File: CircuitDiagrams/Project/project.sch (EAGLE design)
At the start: 105 parts, among them IC1 UC3C, IC2 PCA9542A, IC3 MT48LC4M16A2TSOP54, IC4 TB6593FNGSSOP20, IC5 TB6593FNGSSOP20, J2 1BY2THROUGHHOLE, J3 1BY2THROUGHHOLE, J4 1BY2THROUGHHOLE, Q1 OV7670, Q2 OV7670, Q3 VREGSOT-223, Q4 TCRT1010TH, Q5 TCRT1010TH, Q6 CSM-7X-DU, X2 MICROSDSMD

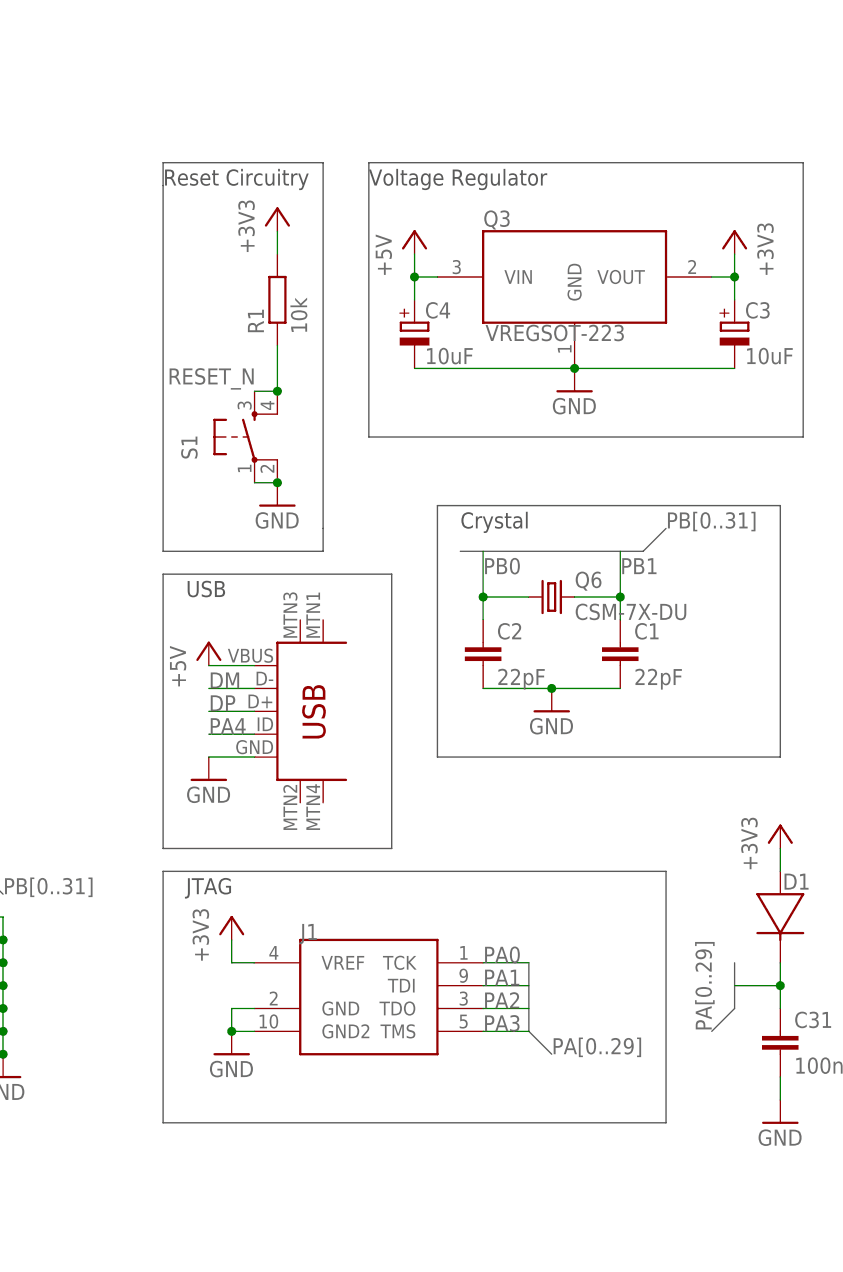
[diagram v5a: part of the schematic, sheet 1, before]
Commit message: Changed JTAG Connection to include the Reset Pin.
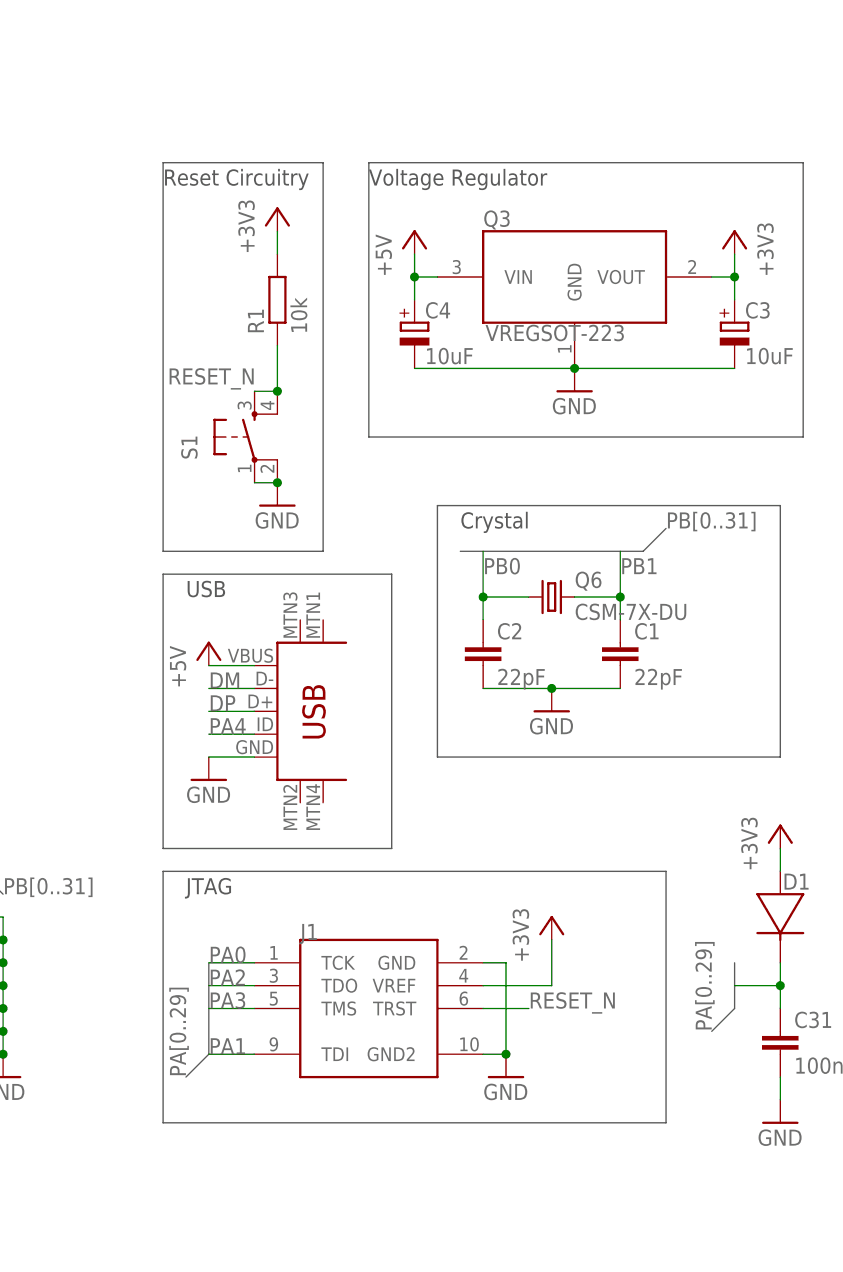
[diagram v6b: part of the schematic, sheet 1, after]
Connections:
- net RESET_N: now also J1.TRST
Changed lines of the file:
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@@
 <text x="134.62" y="60.96" size="1.778" layer="97">USB</text>
 <wire x1="132.08" y1="109.22" x2="149.86" y2="109.22" width="0.1524" layer="97"/>
-<wire x1="149.86" y1="109.22" x2="149.86" y2="68.58" width="0.1524" layer="97"/>
-<wire x1="149.86" y1="68.58" x2="149.86" y2="66.04" width="0.1524" layer="97"/>
+<wire x1="149.86" y1="109.22" x2="149.86" y2="66.04" width="0.1524" layer="97"/>
 <wire x1="149.86" y1="66.04" x2="132.08" y2="66.04" width="0.1524" layer="97"/>
-<wire x1="132.08" y1="66.04" x2="132.08" y2="106.68" width="0.1524" layer="97"/>
-<wire x1="132.08" y1="106.68" x2="132.08" y2="109.22" width="0.1524" layer="97"/>
+<wire x1="132.08" y1="66.04" x2="132.08" y2="109.22" width="0.1524" layer="97"/>
 <text x="132.08" y="106.68" size="1.778" layer="97">Reset Circuitry</text>
 <wire x1="154.94" y1="109.22" x2="203.2" y2="109.22" width="0.1524" layer="97"/>
@@
 <instance part="IC1" gate="G$1" x="50.8" y="58.42"/>
 <instance part="J1" gate="G$1" x="154.94" y="17.78"/>
-<instance part="+3V1" gate="G$1" x="139.7" y="25.4"/>
+<instance part="+3V1" gate="G$1" x="175.26" y="25.4"/>
 <instance part="+3V2" gate="G$1" x="-10.16" y="111.76"/>
 <instance part="GND1" gate="1" x="114.3" y="7.62"/>
-<instance part="GND2" gate="1" x="139.7" y="10.16"/>
+<instance part="GND2" gate="1" x="170.18" y="7.62"/>
 <instance part="U$1" gate="G$1" x="144.78" y="43.18"/>
 <instance part="GND3" gate="1" x="137.16" y="40.64"/>
@@
 </segment>
 <segment>
-<wire x1="172.72" y1="20.32" x2="172.72" y2="12.7" width="0.762" layer="92"/>
-<wire x1="172.72" y1="12.7" x2="175.26" y2="10.16" width="0.762" layer="92"/>
-<label x="175.26" y="10.16" size="1.778" layer="95"/>
+<wire x1="137.16" y1="20.32" x2="137.16" y2="10.16" width="0.762" layer="92"/>
+<wire x1="137.16" y1="10.16" x2="134.62" y2="7.62" width="0.762" layer="92"/>
+<label x="134.62" y="7.62" size="1.778" layer="95" rot="R90"/>
 </segment>
 <segment>
@@
 <nets>
 <net name="GND" class="0">
-<segment>
-<pinref part="J1" gate="G$1" pin="GND"/>
-<pinref part="GND2" gate="1" pin="GND"/>
-<wire x1="142.24" y1="15.24" x2="139.7" y2="15.24" width="0.1524" layer="91"/>
-<wire x1="139.7" y1="15.24" x2="139.7" y2="12.7" width="0.1524" layer="91"/>
-<pinref part="J1" gate="G$1" pin="GND2"/>
-<wire x1="142.24" y1="12.7" x2="139.7" y2="12.7" width="0.1524" layer="91"/>
-<junction x="139.7" y="12.7"/>
-</segment>
 <segment>
 <pinref part="IC1" gate="G$1" pin="GNDIO1"/>
@@
 <wire x1="200.66" y1="5.08" x2="200.66" y2="7.62" width="0.1524" layer="91"/>
 </segment>
+<segment>
+<pinref part="J1" gate="G$1" pin="GND2"/>
+<pinref part="GND2" gate="1" pin="GND"/>
+<wire x1="167.64" y1="10.16" x2="170.18" y2="10.16" width="0.1524" layer="91"/>
+<pinref part="J1" gate="G$1" pin="GND"/>
+<wire x1="167.64" y1="20.32" x2="170.18" y2="20.32" width="0.1524" layer="91"/>
+<wire x1="170.18" y1="20.32" x2="170.18" y2="10.16" width="0.1524" layer="91"/>
+<junction x="170.18" y="10.16"/>
+</segment>
 </net>
 <net name="+3V3" class="0">
@@
 <pinref part="+3V1" gate="G$1" pin="+3V3"/>
 <pinref part="J1" gate="G$1" pin="VREF"/>
-<wire x1="139.7" y1="22.86" x2="139.7" y2="20.32" width="0.1524" layer="91"/>
-<wire x1="139.7" y1="20.32" x2="142.24" y2="20.32" width="0.1524" layer="91"/>
+<wire x1="175.26" y1="22.86" x2="175.26" y2="17.78" width="0.1524" layer="91"/>
+<wire x1="175.26" y1="17.78" x2="167.64" y2="17.78" width="0.1524" layer="91"/>
 </segment>
 <segment>
@@
 <segment>
 <pinref part="J1" gate="G$1" pin="TCK"/>
-<wire x1="167.64" y1="20.32" x2="172.72" y2="20.32" width="0.1524" layer="91"/>
-<label x="167.64" y="20.32" size="1.778" layer="95"/>
+<wire x1="137.16" y1="20.32" x2="142.24" y2="20.32" width="0.1524" layer="91"/>
+<label x="137.16" y="20.32" size="1.778" layer="95"/>
 </segment>
 </net>
@@
 <segment>
 <pinref part="J1" gate="G$1" pin="TDI"/>
-<wire x1="167.64" y1="17.78" x2="172.72" y2="17.78" width="0.1524" layer="91"/>
-<label x="167.64" y="17.78" size="1.778" layer="95"/>
+<wire x1="142.24" y1="10.16" x2="137.16" y2="10.16" width="0.1524" layer="91"/>
+<label x="137.16" y="10.16" size="1.778" layer="95"/>
 </segment>
 </net>
@@
 <segment>
 <pinref part="J1" gate="G$1" pin="TDO"/>
-<wire x1="167.64" y1="15.24" x2="172.72" y2="15.24" width="0.1524" layer="91"/>
-<label x="167.64" y="15.24" size="1.778" layer="95"/>
+<wire x1="142.24" y1="17.78" x2="137.16" y2="17.78" width="0.1524" layer="91"/>
+<label x="137.16" y="17.78" size="1.778" layer="95"/>
 </segment>
 </net>
@@
 <segment>
 <pinref part="J1" gate="G$1" pin="TMS"/>
-<wire x1="172.72" y1="12.7" x2="167.64" y2="12.7" width="0.1524" layer="91"/>
-<label x="167.64" y="12.7" size="1.778" layer="95"/>
+<wire x1="142.24" y1="15.24" x2="137.16" y2="15.24" width="0.1524" layer="91"/>
+<label x="137.16" y="15.24" size="1.778" layer="95"/>
 </segment>
 </net>
@@
 <label x="132.588" y="84.582" size="1.778" layer="95"/>
 </segment>
-</net>
+<segment>
+<pinref part="J1" gate="G$1" pin="TRST"/>
+<wire x1="167.64" y1="15.24" x2="172.72" y2="15.24" width="0.1524" layer="91"/>
+<label x="172.72" y="15.24" size="1.778" layer="95"/>
+</segment>
+</net>

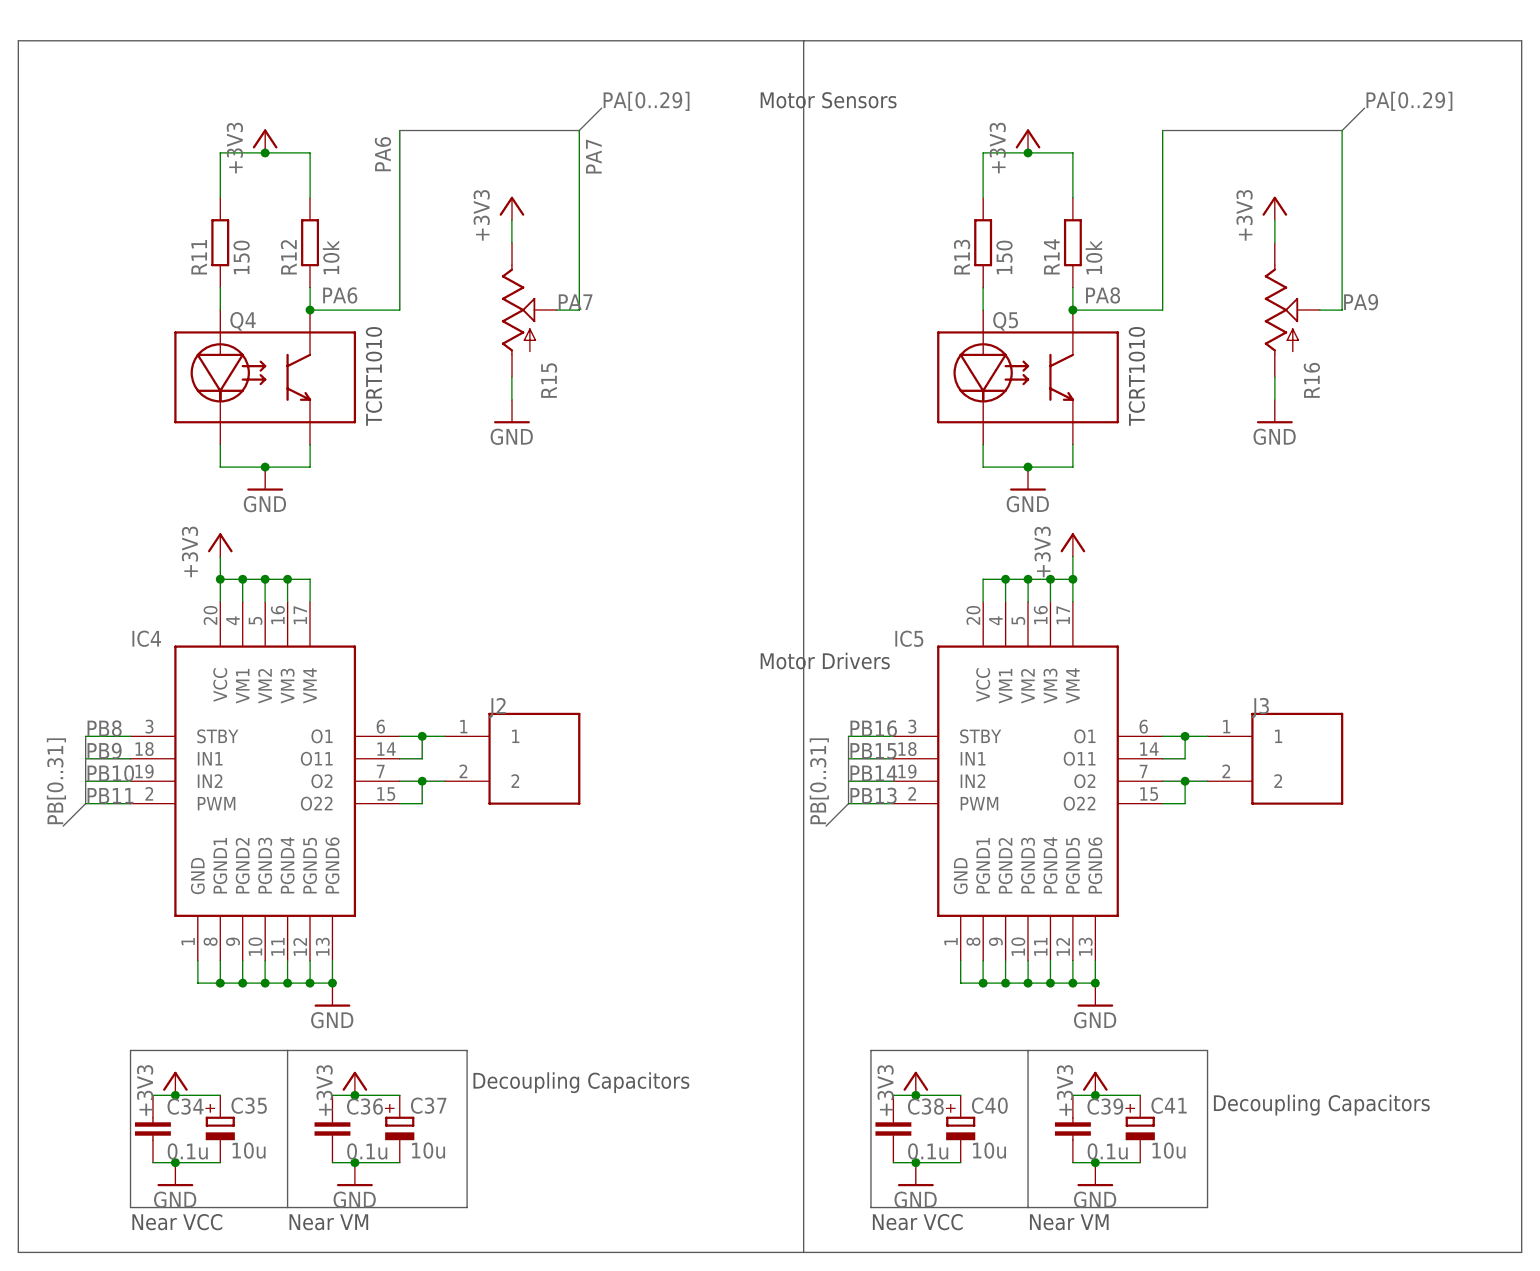
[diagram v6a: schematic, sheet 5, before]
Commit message: Added LEDs to the deisgn and a USART Port.
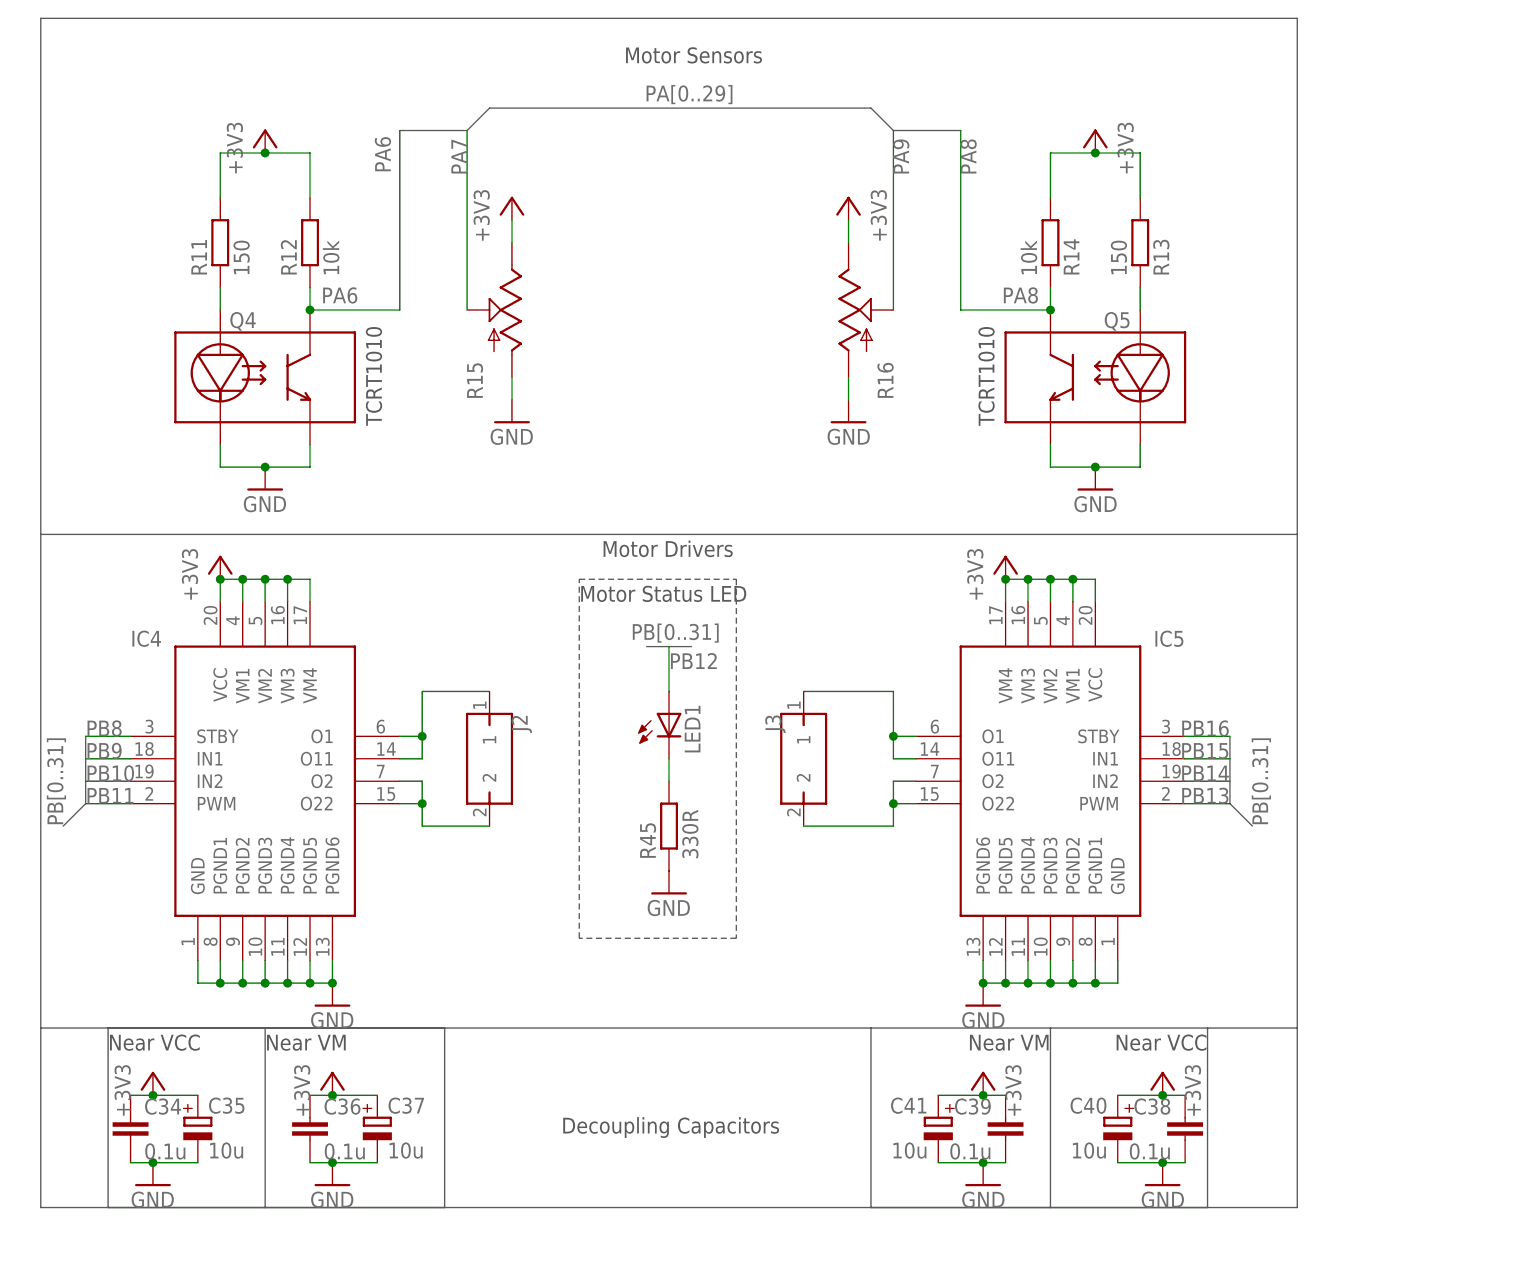
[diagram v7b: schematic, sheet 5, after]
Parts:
- added J5: 8PIN1.27MM2X4TH, Headers:8PIN1.27MM2X4TH
- added J6: 4PIN1.27MM2X2TH, Headers:4PIN1.27MM2X2TH
- added J7: 1BY2THROUGHHOLE, Headers:1BY2THROUGHHOLE
- added LED1, LED2, LED3, LED4, LED5, LED6: (no value), Semiconductors:LED1206
- added R44, R45, R46, R47, R48, R49: 330R, passives:R0603
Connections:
- new net N$30: LED2.C, R44.2
- new net N$31: LED1.C, R45.2
- new net N$32: LED3.C, R46.2
- new net N$33: LED4.C, R47.2
- new net N$34: LED5.C, R48.2
- new net N$35: LED6.C, R49.2
- net +3V3: now also J6.1
- net +5V: now also J6.4
- net GND: now also J6.2, J6.3, R44.1, R45.1, R46.1, R47.1, R48.1, R49.1
- net PB12: now also LED1.A
- net PB17: now also LED2.A
- net PB18: now also LED3.A
- net PB19: now also J5.1
- net PB20: now also J5.2
- net PB21: now also J5.3
- net PB22: now also J5.5
- net PB23: now also J5.6
- net PB24: now also J5.7
- net PB25: now also J5.8
- net PB27: now also LED4.A
- net PB28: now also LED5.A
- net PB29: now also LED6.A
- net PC18: now also IC3.A10
- net PC4: now also J7.1
- net PC5: now also J7.2
- net PD10: now also IC3.A5; no longer IC3.A7
- net PD11: now also IC3.A6; no longer IC3.A8
- net PD12: now also IC3.A7; no longer IC3.A9
- net PD14: now also IC3.A8; no longer IC3.A10
- net PD15: now also IC3.A9; no longer IC3.A11
- net PD16: no longer IC3.BA1
- net PD17: now also IC3.A11; no longer IC3.BA0
- net PD20: now also IC3.BA0
- net PD21: now also IC3.BA1
- net PD24: now also IC3.DQMH
- net PD3: now also IC3.DQML; no longer IC3.A0
- net PD4: no longer IC3.A1
- net PD5: now also IC3.A0; no longer IC3.A2
- net PD6: now also IC3.A1; no longer IC3.A3
- net PD7: now also IC3.A2; no longer IC3.A4
- net PD8: now also IC3.A3; no longer IC3.A5
- net PD9: now also IC3.A4; no longer IC3.A6
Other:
- note added: "1 - 3V3 2 - GND 3 - GND 4 - 5V"
- note added: "1 - MOSI 2 - MISO 3 - SCK 4 - NC 5 - CS3 6 - CS2 7 - CS1 8 - CS0"
- note added: "1 - SDA 2 - SCL"
- note added: "1- TXD 2 - RXD"
- note added: "LEDs"
- note added: "Motor Status LED"
- note added: "Power Test Point"
- note added: "SPI Test Point"
- note added: "USART Test Point"
- moved on the sheet: C34, C35, C36, C37, C38, C39, C40, C41, IC5, Q5, R13, R14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

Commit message: Completed First Draft of Schematic
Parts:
- added J8: 10PIN1.27MM2X5TH, Headers:10PIN1.27MM2X5TH
- added LED7: (no value), Semiconductors:LED1206
- added R50: 330R, passives:R0603
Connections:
- removed net OVDATA0: Q1.D0, Q2.D0
- removed net OVDATA1: Q1.D1, Q2.D1
- removed net OVDATA2: Q1.D2, Q2.D2
- removed net OVDATA3: Q1.D3, Q2.D3
- removed net OVDATA4: Q1.D4, Q2.D4
- removed net OVDATA5: Q1.D5, Q2.D5
- removed net OVDATA6: Q1.D6, Q2.D6
- removed net OVDATA7: Q1.D7, Q2.D7
- removed net PA11: IC1.PA11
- new net N$36: LED7.C, R50.2
- net +3V3: now also LED7.A; no longer C5.1, C6.1
- net GND: now also R50.1
- net PA10: now also J8.2
- net PA12: now also J8.3
- net PA13: now also J8.4
- net PA14: now also J8.5
- net PA16: now also IC1.PA11
- net PA5: now also J8.1
- net PB0: now also Q1.D0, Q2.D0; no longer C2.1, Q6.1
- net PB1: now also Q1.D1, Q2.D1; no longer C1.1, Q6.2
- net PB2: now also Q1.D2, Q2.D2
- net PB3: now also Q1.D3, Q2.D3
- net PB30: now also C2.1, Q6.1
- net PB31: now also C1.1, Q6.2
- net PB4: now also Q1.D4, Q2.D4
- net PB5: now also Q1.D5, Q2.D5
- net PB6: now also Q1.D6, Q2.D6
- net PB7: now also Q1.D7, Q2.D7
- net PC0: now also J8.10
- net PC1: now also J8.9
- net PC13: now also J8.7
- net PC6: now also J8.8
- net PD29: now also J8.6
- net VDDCORE: now also C5.1, C6.1
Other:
- note added: "Analogue Reference"
- note added: "Close to VDDCORE/GNDCORE"
- note added: "Near VDD / GND of Camera 0"
- note added: "Near VDD / GND of Camera 1"
- note added: "PA11"
- note added: "Power LED"
- note added: "Spare Pins"
- note removed: "Close to VDD/GND CORE"
- moved on the sheet: C1, C10, C11, C12, C13, C14, C15, C16, C17, C18, C19, C2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
